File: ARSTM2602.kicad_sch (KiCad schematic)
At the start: 30 parts, among them J1 Conn_01x03_Pin, J10 Conn_ST_STDC14, J2 Conn_01x03_Pin, J3 Conn_01x03_Pin, J4 Conn_01x03_Pin, J5 Conn_01x03_Pin, J6 Conn_01x03_Pin, J7 Conn_01x03_Pin, J8 Conn_01x02_Socket, J9 Conn_01x02_Socket, SW2 SW_Push, U1 STM32G431RBTx, U2 BD33FC0FP

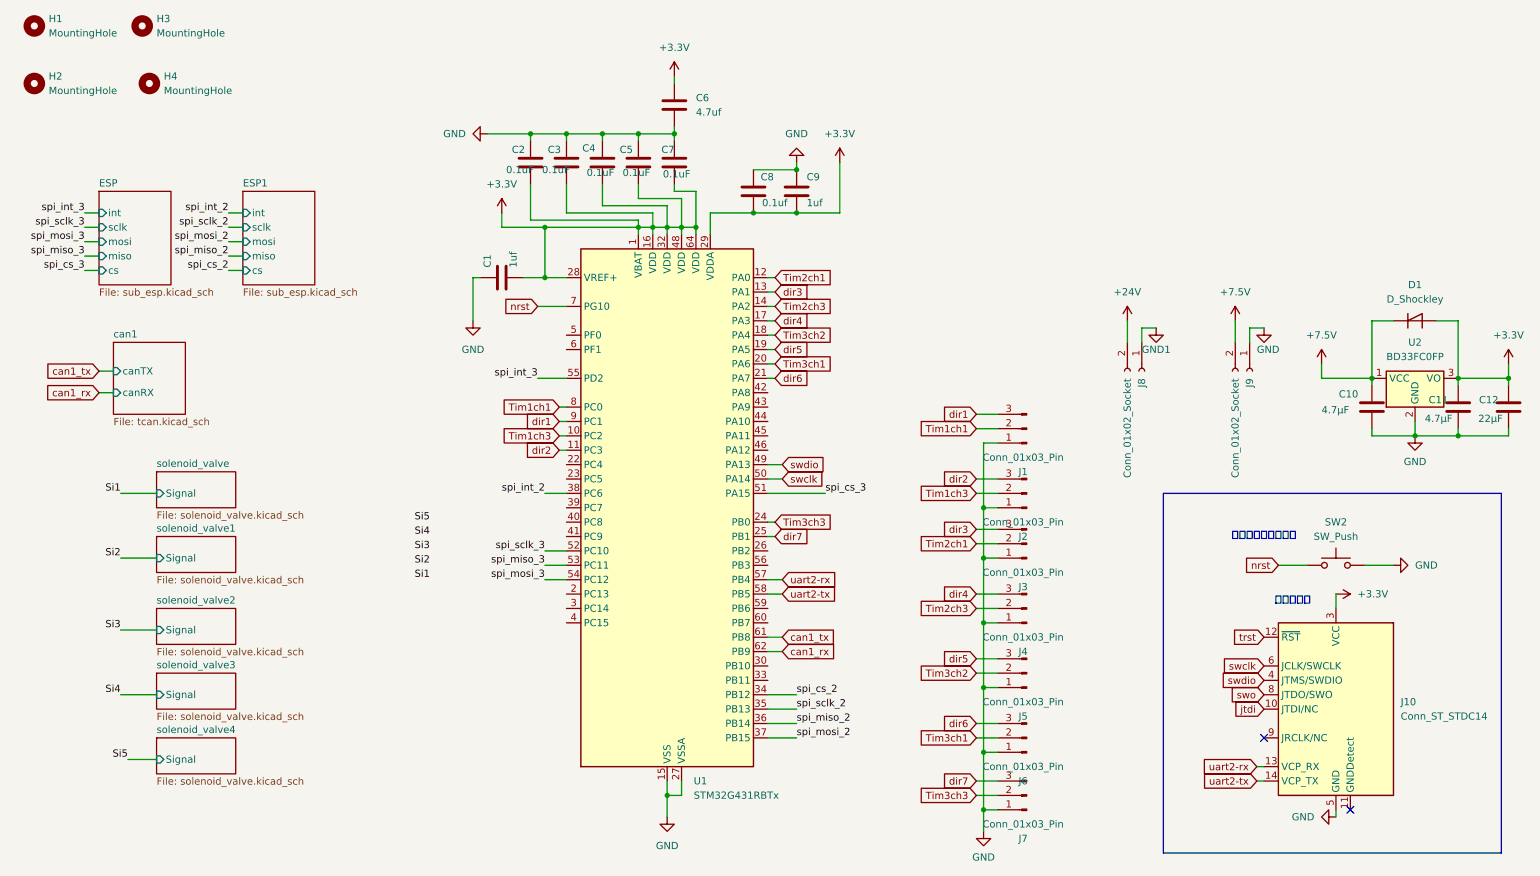
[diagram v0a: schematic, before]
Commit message: サーボときんていをつけ忘れていたので回路図に追加(部品配置に悩んでる
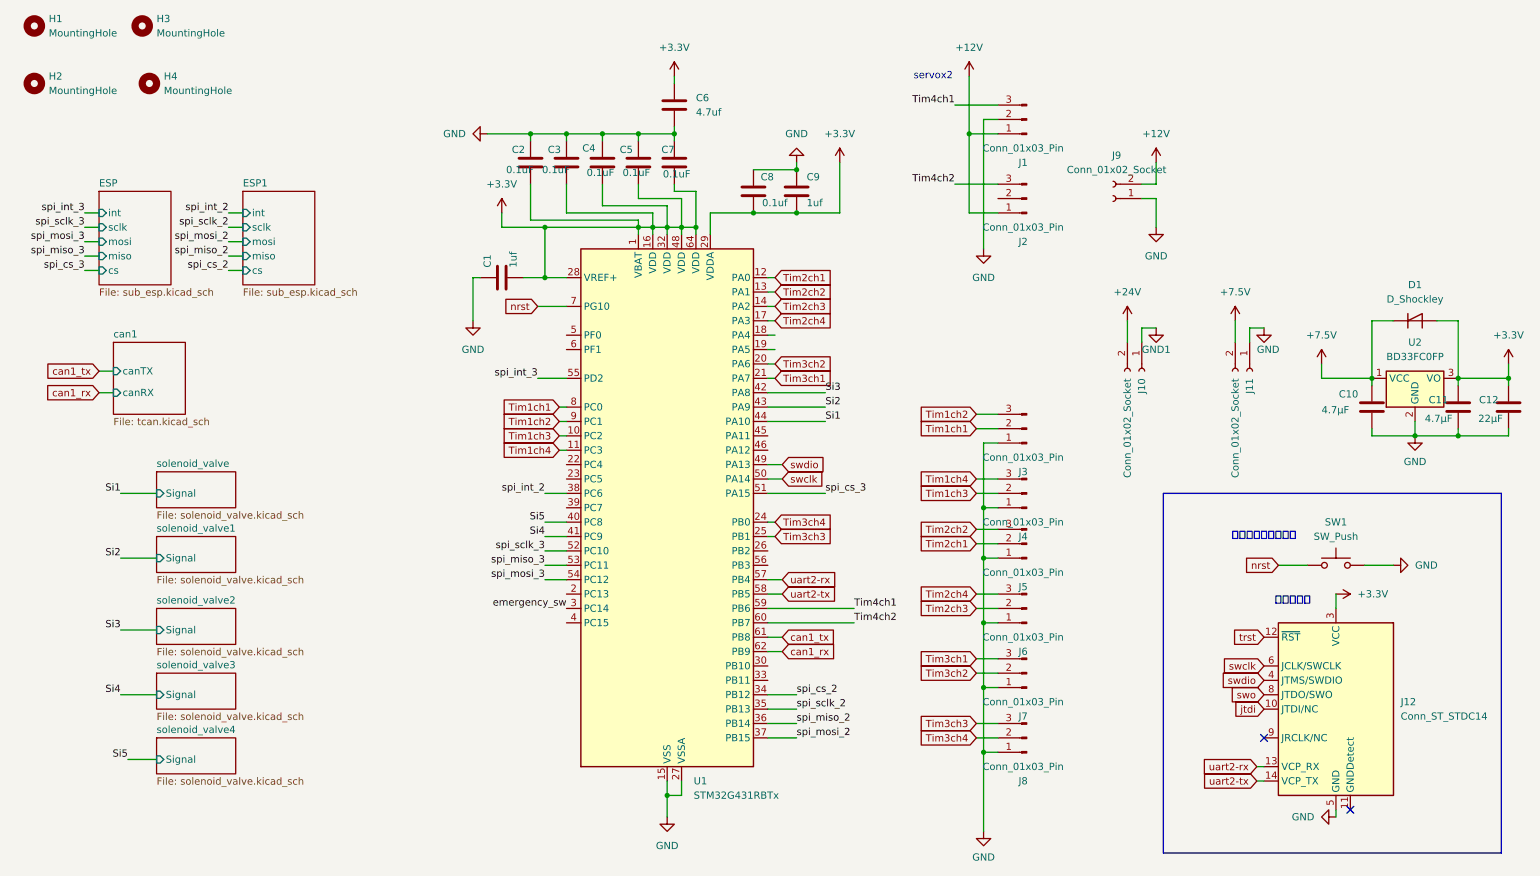
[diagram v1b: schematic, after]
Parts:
- removed J7: Conn_01x03_Pin, Connector_JST:JST_XH_S3B-XH-A-1_1x03_P2.50mm_Horizontal, symbol Connector:Conn_01x03_Pin
- added J1, J2: Conn_01x03_Pin, Connector_JST:JST_XH_S3B-XH-A-1_1x03_P2.50mm_Horizontal, symbol Connector:Conn_01x03_Pin
- added J9: Conn_01x02_Socket, Connector_AMASS:AMASS_XT30PW-M_1x02_P2.50mm_Horizontal, symbol Connector:Conn_01x02_Socket
- renumbered J8 to J10, J9 to J11, J10 to J12, J1 to J3, J2 to J4, J3 to J5, J4 to J6, J5 to J7, J6 to J8, SW2 to SW1
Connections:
- net dir7 is gone; now on net Tim3ch3: U1.25 (PB1)
- net GND: now also J1.2 (Pin_2), J9.1 (Pin_1)
- net Si1: now also U1.44 (PA10)
- net Si2: now also U1.43 (PA9)
- net Si3: now also U1.42 (PA8)
- net Si4: now also U1.41 (PC9)
- net Si5: now also U1.40 (PC8)
- net Tim3ch1: now also J7.3 (Pin_3), U1.21 (PA7); no longer J8.2 (Pin_2), U1.20 (PA6)
- net Tim3ch2: now also U1.20 (PA6); no longer U1.18 (PA4)
- net Tim3ch3: now also J8.3 (Pin_3); no longer U1.24 (PB0)
- net emergency_sw: now reaches U1.3 (PC14)
- net Tim4ch1: now reaches U1.59 (PB6)
- net Tim4ch1: now also J1.3 (Pin_3)
- net Tim4ch2: now reaches U1.60 (PB7)
- net Tim4ch2: now also J2.3 (Pin_3)
- net dir1 renamed Tim1ch2
- net dir2 renamed Tim1ch4
- net dir3 renamed Tim2ch2
- net dir4 renamed Tim2ch4
- net dir5: no longer names the net of U1.19 (PA5)
- net dir5: no longer J7.3 (Pin_3)
- removed net dir6: J8.3 (Pin_3), U1.21 (PA7)
- new net +12V: J1.1 (Pin_1), J2.1 (Pin_1), J9.2 (Pin_2)
- new net Tim3ch4: J8.2 (Pin_2), U1.24 (PB0)
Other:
- note added: "servox2"

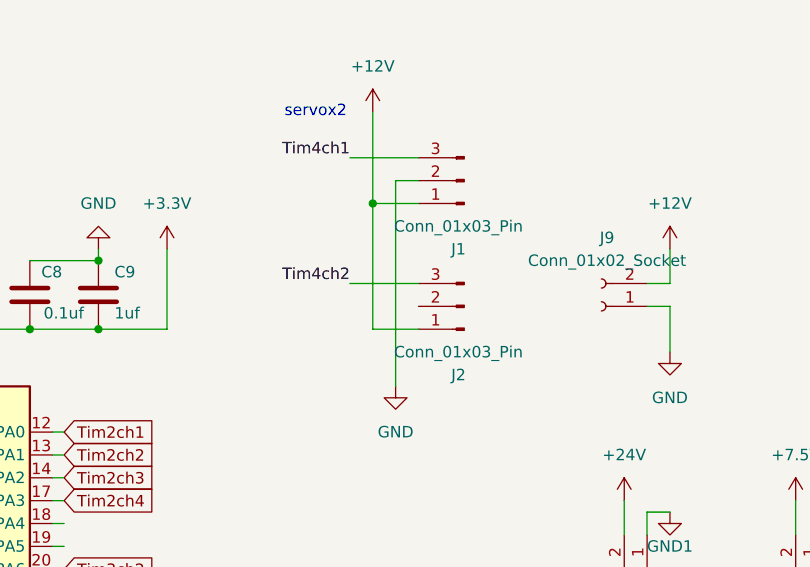
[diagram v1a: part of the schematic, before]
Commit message: サーボ系ときんてい系の部品の配置と配線
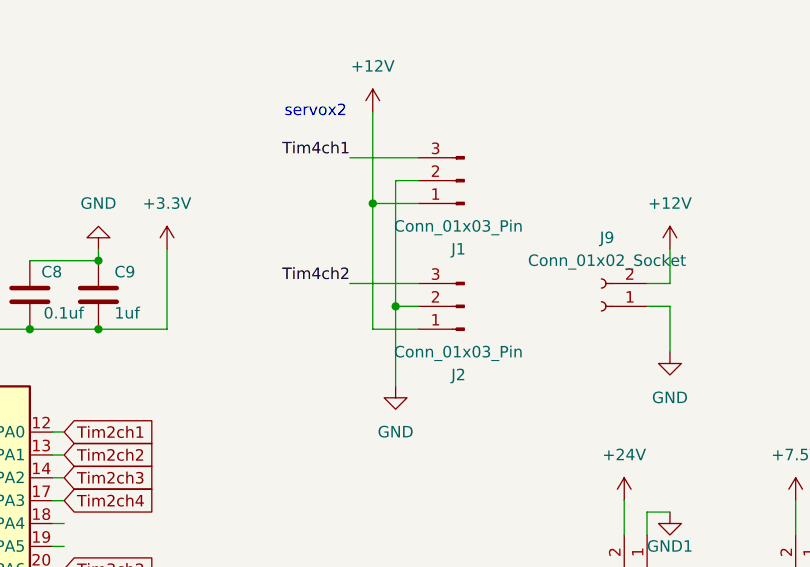
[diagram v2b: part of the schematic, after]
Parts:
- J2, J4, J6: footprint Connector_JST:JST_XH_S3B-XH-A-1_1x03_P2.50mm_Horizontal -> Connector_JST:JST_XH_B3B-XH-A_1x03_P2.50mm_Vertical
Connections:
- net GND: now also J2.2 (Pin_2)
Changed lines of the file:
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@@
 	)
 	(junction
+		(at 185.42 48.26)
+		(diameter 0)
+		(color 0 0 0 0)
+	)
+	(junction
 		(at 105.41 36.83)
 		(diameter 0)
@@
 	(wire
 		(pts
+			(xy 185.42 48.26) (xy 185.42 57.15)
+		)
+		(stroke
+			(width 0)
+			(type default)
+		)
+	)
+	(wire
+		(pts
 			(xy 147.32 118.11) (xy 149.86 118.11)
 		)
@@
 	(wire
 		(pts
+			(xy 185.42 48.26) (xy 187.96 48.26)
+		)
+		(stroke
+			(width 0)
+			(type default)
+		)
+	)
+	(wire
+		(pts
 			(xy 233.68 148.59) (xy 234.95 148.59)
 		)
@@
 	(wire
 		(pts
-			(xy 185.42 34.29) (xy 185.42 57.15)
+			(xy 185.42 34.29) (xy 185.42 48.26)
 		)
 		(stroke
@@
 			)
 		)
-		(property "Footprint" "Connector_JST:JST_XH_S3B-XH-A-1_1x03_P2.50mm_Horizontal"
+		(property "Footprint" "Connector_JST:JST_XH_B3B-XH-A_1x03_P2.50mm_Vertical"
 			(at 193.04 120.65 0)
 			(hide yes)
@@
 			)
 		)
-		(property "Footprint" "Connector_JST:JST_XH_S3B-XH-A-1_1x03_P2.50mm_Horizontal"
+		(property "Footprint" "Connector_JST:JST_XH_B3B-XH-A_1x03_P2.50mm_Vertical"
 			(at 193.04 48.26 0)
 			(hide yes)
@@
 			)
 		)
-		(property "Footprint" "Connector_JST:JST_XH_S3B-XH-A-1_1x03_P2.50mm_Horizontal"
+		(property "Footprint" "Connector_JST:JST_XH_B3B-XH-A_1x03_P2.50mm_Vertical"
 			(at 193.04 100.33 0)
 			(hide yes)
